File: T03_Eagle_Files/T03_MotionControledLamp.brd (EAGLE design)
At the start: 100 x 80 mm, 27 parts, among them IC1 L7805, SW1 RESET, U1 ATMEGA328P-MU, U4 TPS61161ADRVT, X2 16MHz

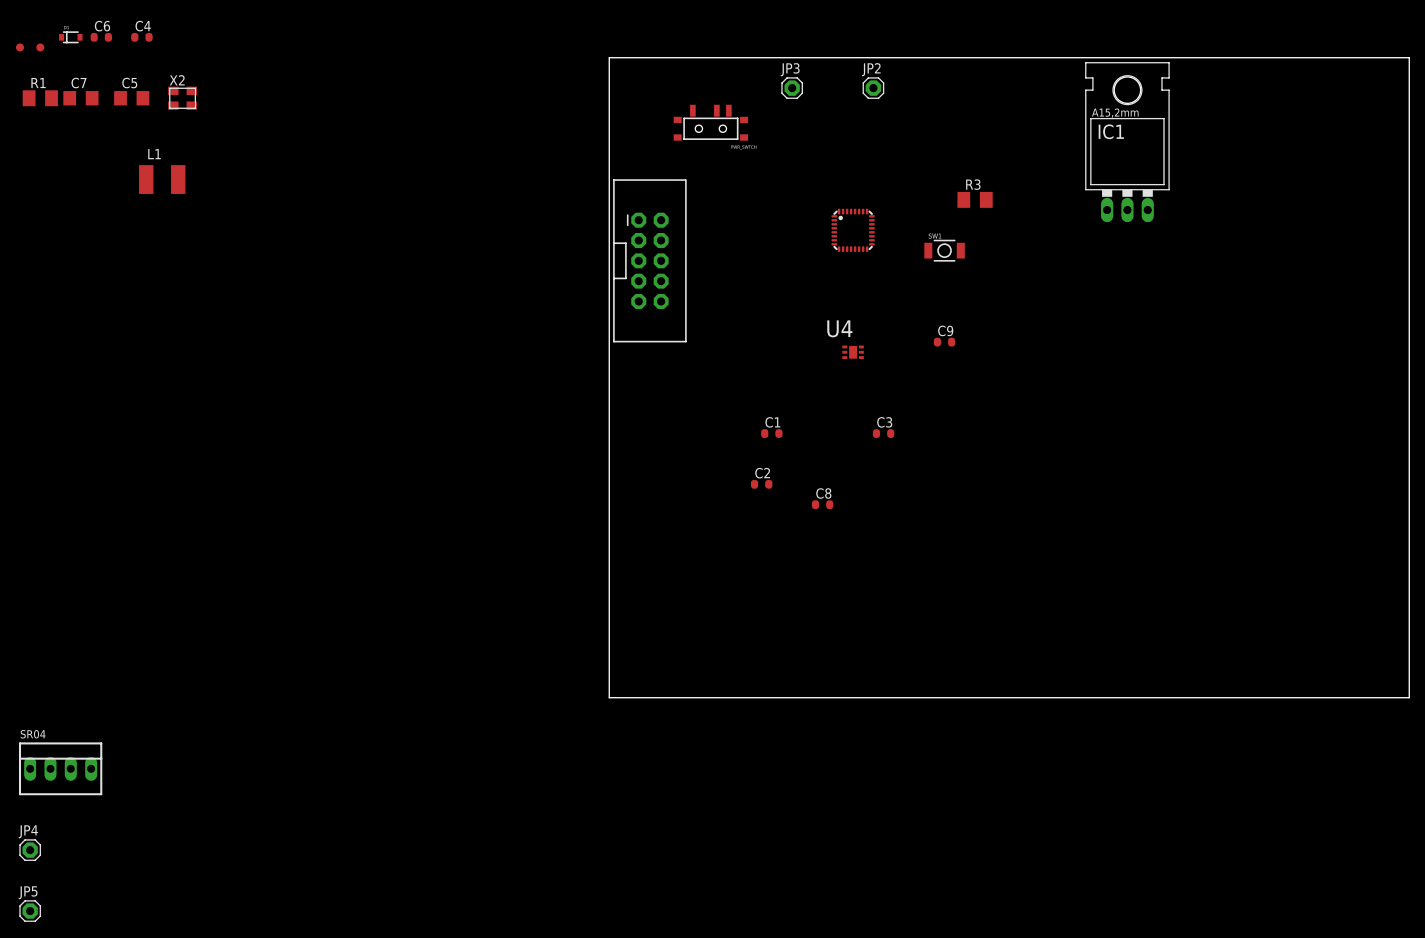
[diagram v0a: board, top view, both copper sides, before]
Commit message: Started routing. Has polygon ready. Just ratsnest and then name the polygon to GND
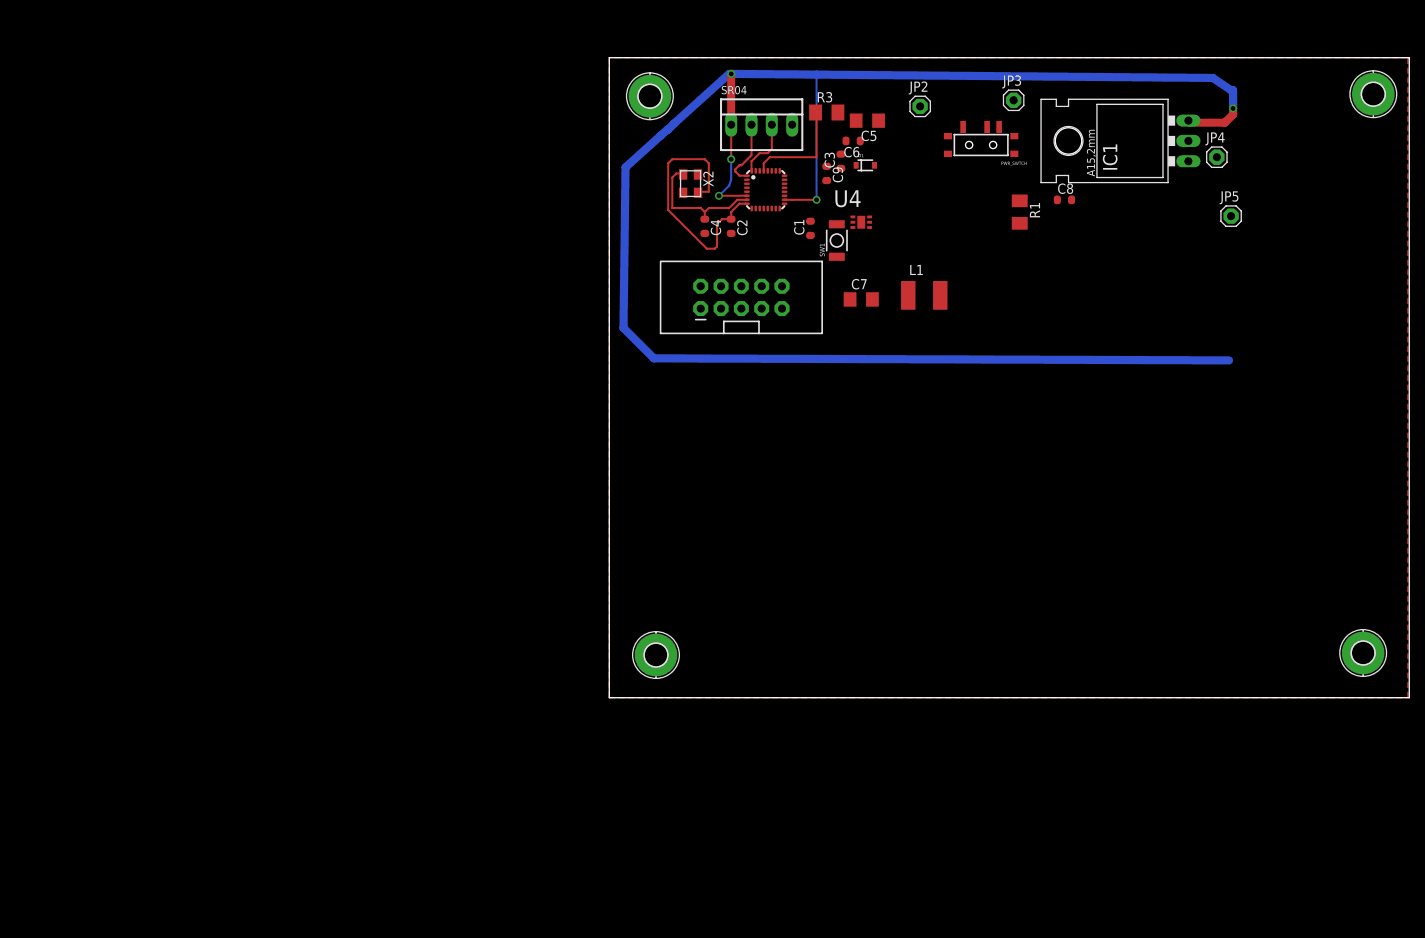
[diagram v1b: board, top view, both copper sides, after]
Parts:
- removed U$2, U$4: FIDUCIAL1X2, SparkFun:FIDUCIAL-1X2
- added H1, H2, H3, H4: MOUNT-PAD-ROUND2.8, holes:2,8-PAD
- moved JP5 173.4 mm to (77.7, 60.2)
- moved JP4 171.8 mm to (75.9, 67.6)
- moved R1 123.3 mm to (51.3, 60.7), turned to 270 degrees
- moved SR04 119.0 mm to (19.1, 71.6)
- moved C7 100.7 mm to (31.5, 49.8)
- moved D1 100.6 mm to (32.0, 66.5)
- moved L1 96.3 mm to (39.4, 50.3)
- moved C6 94.9 mm to (30.5, 69.6), turned to 180 degrees
- moved C5 92.0 mm to (32.3, 72.1), turned to 180 degrees
- moved C4 74.2 mm to (11.9, 58.9), turned to 270 degrees
- moved X2 64.4 mm to (10.2, 64.3), turned to 270 degrees
- moved C8 48.6 mm to (56.9, 62.2)
- moved C3 34.5 mm to (29.0, 67.1), turned to 90 degrees
- moved PWR_SWTCH 33.8 mm to (46.5, 69.1)
- moved C2 32.5 mm to (15.2, 58.9), turned to 270 degrees
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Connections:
- net N$1 renamed XTAL1
- net N$2 renamed XTAL2
- new net ECHO: SR04.3, U1.32
- new net TRIG: SR04.2, U1.1
- net MISO: no longer SR04.2
- net MOSI: no longer SR04.3
- net N$6: now also JP4.1
- net NC: no longer U1.1, U1.32
- net RST: no longer JP1.7
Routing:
- net +5V: track 0.00 -> 226.8 mm, vias 0 -> 5
- net XTAL2: track 0.00 -> 32.6 mm
- net XTAL1: track 0.00 -> 16.6 mm
- net RST: track 0.00 -> 13.5 mm
- net TRIG: track 0.00 -> 8.51 mm
- net ECHO: track 0.00 -> 7.44 mm
- added copper zone on layer 1, net GND

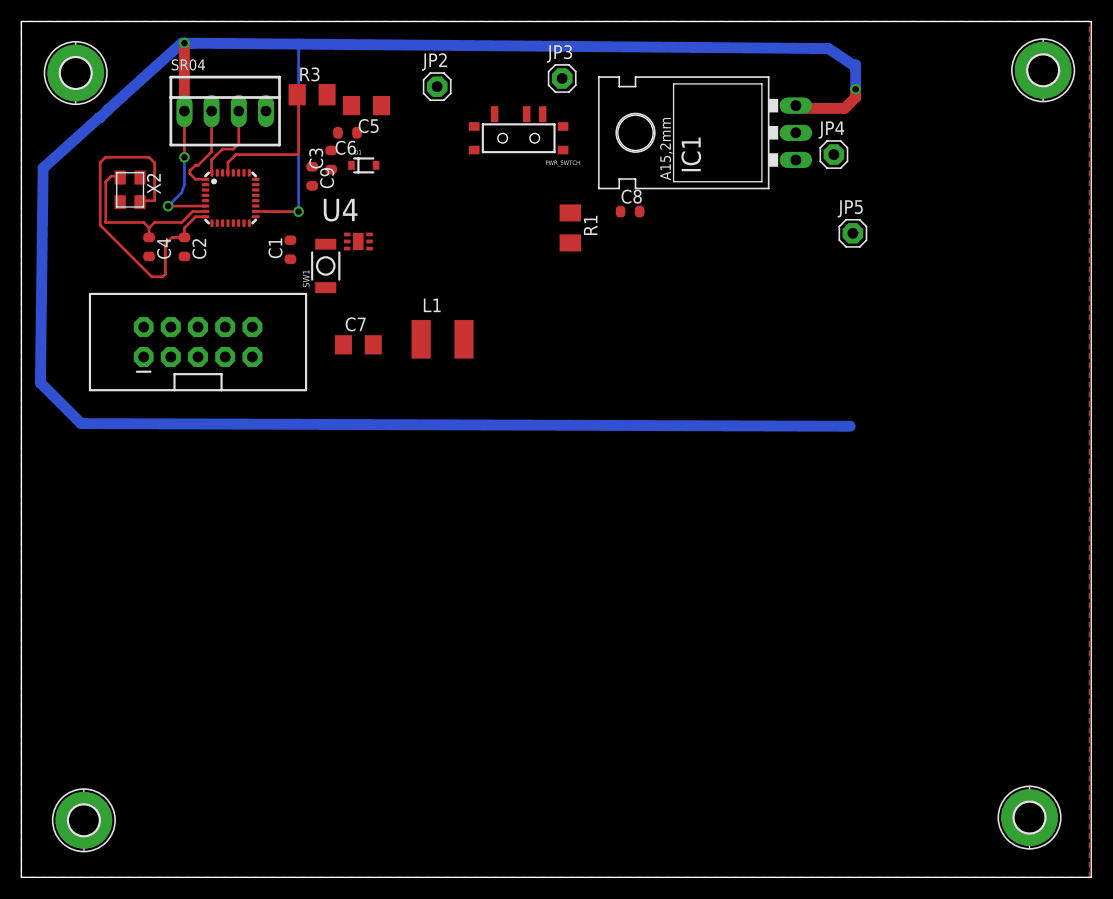
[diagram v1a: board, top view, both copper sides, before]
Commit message: Completed Board Layout First Draft
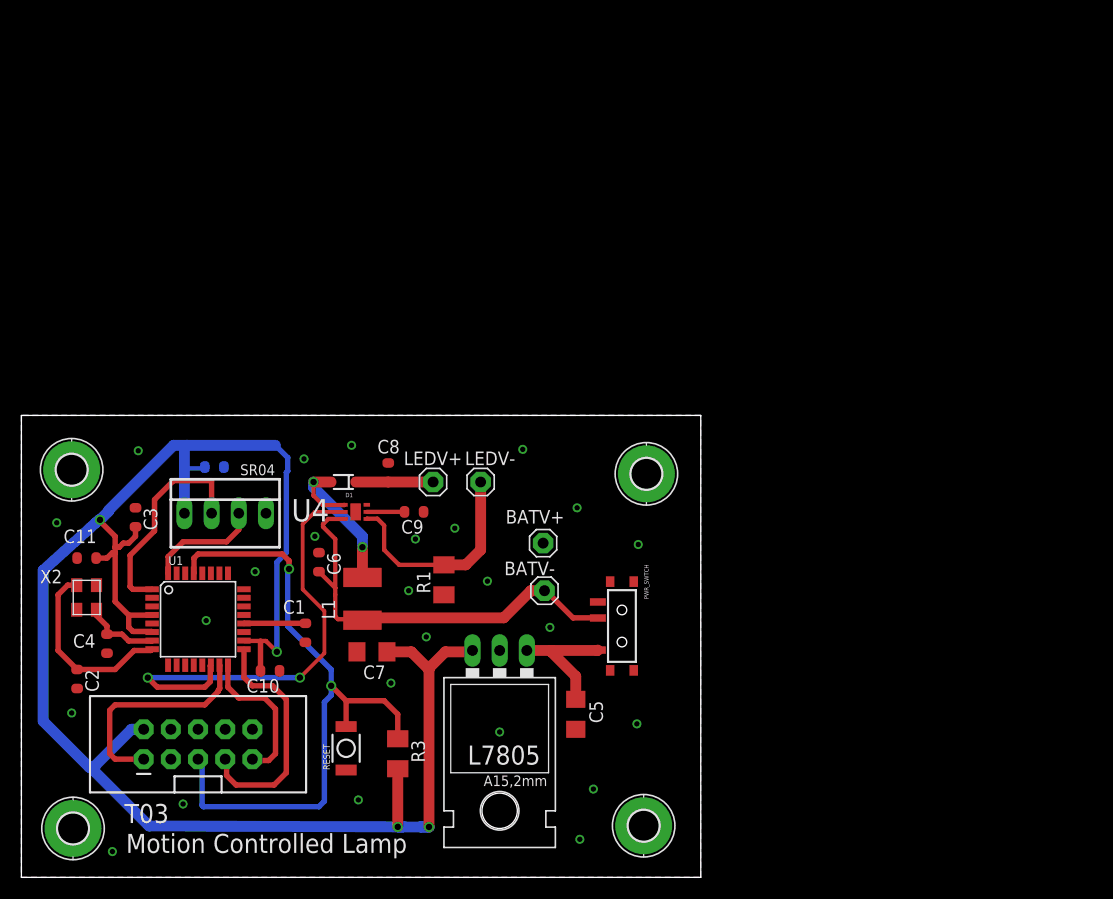
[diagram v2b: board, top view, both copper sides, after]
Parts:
- removed IC1: L7805, v-reg:78XXL
- removed JP2: BAT_POS_VOLT, adafruit:1X01
- removed JP3: BAT_GND, adafruit:1X01
- removed JP4: LED_V+, adafruit:1X01
- removed JP5: LED_V-, adafruit:1X01
- removed SW1: RESET, Smartprj:SMD_157SW
- added BATV+: BAT_GND, adafruit:1X01
- added BATV-: BAT_POS_VOLT, adafruit:1X01
- added C10, C11, C12: 0.1uF, Smartprj:C0603-ROUND
- added L7805: L7805, v-reg:78XXL
- added LEDV+: LED_V+, adafruit:1X01
- added LEDV-: LED_V-, adafruit:1X01
- added RESET: RESET, Smartprj:SMD_157SW
- U1: device Smartprj:MLF32-M1-A -> Smartprj:TQFP32-08
- moved R3 62.1 mm to (35.2, 11.6), turned to 270 degrees
- moved C5 60.2 mm to (51.8, 15.2), turned to 270 degrees
- moved H3 52.9 mm to (58.4, 37.7)
- moved PWR_SWTCH 46.6 mm to (56.1, 23.5), turned to 90 degrees
- moved C2 41.6 mm to (5.21, 18.5)
- moved C6 40.2 mm to (27.8, 29.5), turned to 270 degrees
- moved U1 39.5 mm to (16.5, 24.1)
- moved X2 38.3 mm to (6.10, 26.2), turned to 90 degrees
- moved C3 38.1 mm to (10.7, 33.7), turned to 270 degrees
- moved JP1 37.6 mm to (16.5, 12.4)
- moved SR04 37.6 mm to (19.1, 34.0)
- moved C4 37.3 mm to (8.00, 21.8)
- moved H4 37.1 mm to (4.70, 38.1)
- moved H2 36.1 mm to (58.2, 4.83)
- moved C1 35.8 mm to (26.5, 22.9)
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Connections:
- net N$13 renamed COMP
- net N$3 renamed SW
- removed net N$14: JP5.1, R1.2, U4.1
- removed net N$6: C8.2, D1.C, JP4.1
- removed net NC: U1.10, U1.11, U1.12, U1.13, U1.19, U1.2, U1.22, U1.23, U1.24, U1.25, U1.26, U1.27, U1.28, U1.9
- new net ADC6: U1.19
- new net ADC7: U1.22
- new net FB: LEDV-.1, R1.2, U4.1
- new net LED_V+: C8.2, D1.C, LEDV+.1
- new net PB0: U1.12
- new net PB1: U1.13
- new net PC0: U1.23
- new net PC1: U1.24
- new net PC2: U1.25
- new net PC3: U1.26
- new net PC4: U1.27
- new net PC5: U1.28
- new net PD4: U1.2
- new net PD5: U1.9
- new net PD6: U1.10
- new net PD7: U1.11
- new net SCK: JP1.7, U1.17
- net +5V: now also C10.2, C11.2, C12.2, L7805.OUT; no longer C6.2, IC1.OUT, L1.1, U4.6
- net +V_BAT: now also BATV-.1, C6.2, L1.1, U4.6; no longer JP2.1
- net GND: now also BATV+.1, C10.1, C11.1, C12.1, L7805.GND, RESET.1; no longer IC1.GND, JP3.1, SW1.1
- net N$4: now also L7805.IN; no longer IC1.IN
- net RST: now also RESET.2; no longer SW1.2, U1.17
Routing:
- net +5V: track 226.8 -> 175.4 mm, vias 5 -> 4
- net RST: track 13.5 -> 63.4 mm, vias 0 -> 2
- net PWM_LEDS: track 0.00 -> 42.7 mm, vias 0 -> 2
- net +V_BAT: track 0.00 -> 40.6 mm
- net SCK: track 0.00 -> 22.3 mm
- net MOSI: track 0.00 -> 20.9 mm
- net FB: track 0.00 -> 20.7 mm
- net SW: track 0.00 -> 17.0 mm, vias 0 -> 2
- net XTAL2: track 32.6 -> 17.6 mm
- net MISO: track 0.00 -> 14.0 mm
- net N$4: track 0.00 -> 12.2 mm
- net TRIG: track 8.51 -> 20.4 mm
- net XTAL1: track 16.6 -> 7.18 mm
- net LED_V+: track 0.00 -> 7.23 mm
- net AREF: track 0.00 -> 5.75 mm
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- added copper zone on layer 16, net GND
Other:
- board size 100 x 80 mm -> 63.5 x 43.2 mm
- board text added: "Motion Controlled Lamp"
- board text added: "T03"
